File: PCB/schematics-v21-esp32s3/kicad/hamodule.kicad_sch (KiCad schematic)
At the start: 84 parts, among them J1 GND|5V, J10 Conn_01x02_Male, J11 2604-1104, J12 2604-1104, J13 EspSense, J2 Conn_01x02_Male, J3 2604-1102, J4 USB | PS, J5 GND|3.3V, J6 Conn_01x02_Male, J7 Current Jumper, J8 USB_C_Receptacle_USB2.0, J9 EspRelays, K1 AQG12205, K2 AQG12205, K3 AQG12205, K4 AQG12205, SW1 Switch, SW2 Switch, U1 LD1117AV33, U2 ESP32-S3-WROOM-2, U3 USBLC6-2SC6, U4 ULN2003A, U5 LDA210-PDIP, U6 LDA210-PDIP, U7 SHT4x

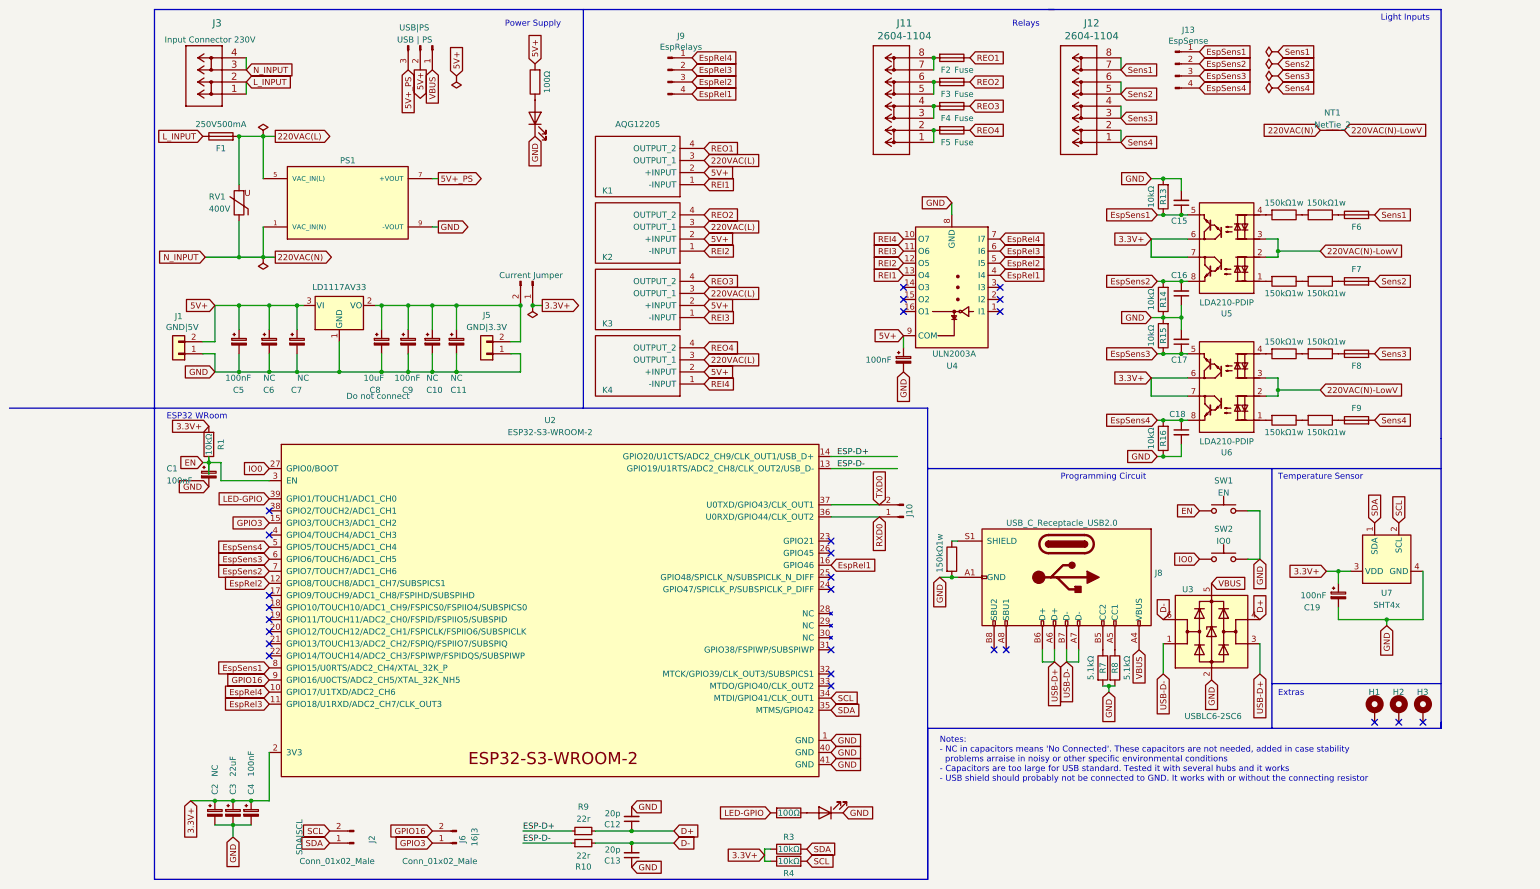
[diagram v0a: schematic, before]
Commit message: [V21] Bring DEPSI back!; expose 3rd GPIO; remove ESP unused libraries;
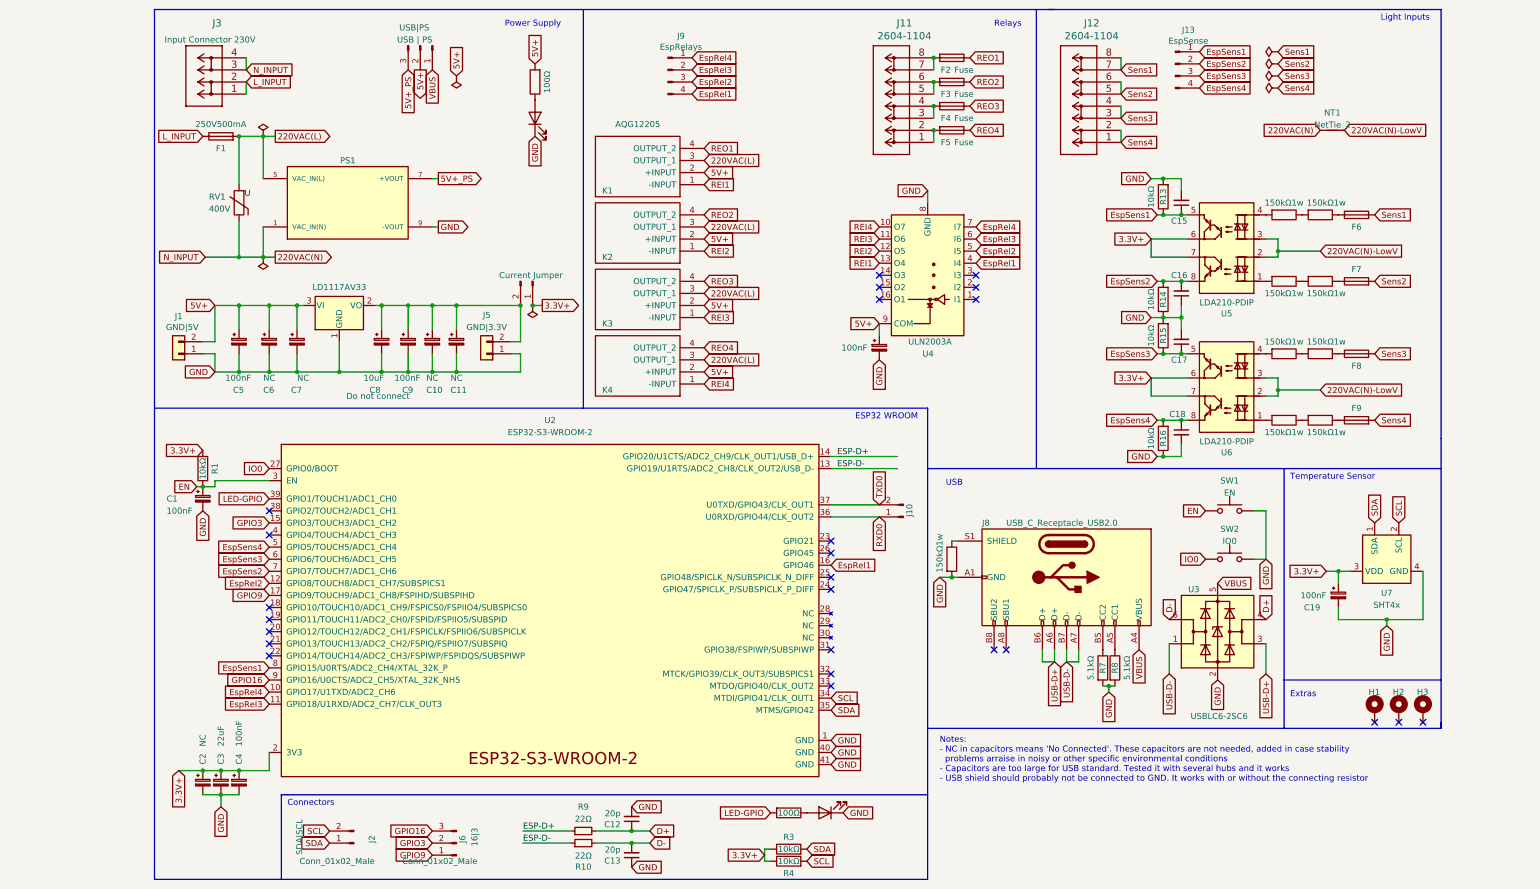
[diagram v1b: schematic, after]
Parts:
- J6: footprint Connector_PinHeader_2.54mm:PinHeader_1x02_P2.54mm_Vertical -> Connector_PinHeader_2.54mm:PinHeader_1x03_P2.54mm_Vertical; symbol Connector:Conn_01x02_Male -> Connector:Conn_01x03_Male
- R10, R9: value 22r -> 22Ω
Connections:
- net GPIO16: now also J6.3 (Pin_3); no longer J6.2 (Pin_2)
- net GPIO3: now also J6.2 (Pin_2); no longer J6.1 (Pin_1)
- net GPIO9: now reaches U2.17 (GPIO9/TOUCH9/ADC1_CH8/FSPIHD/SUBSPIHD)
- net GPIO9: now also J6.1 (Pin_1)
- no-connect marks 26 -> 25
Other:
- note added: "Connectors"
- note added: "ESP32 WROOM"
- note added: "USB"
- note removed: "ESP32 WRoom"
- note removed: "Programming Circuit"
- moved on the sheet: C1, C2, C3, C4, R1, SW1, SW2, U3, U4

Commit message: Images + Gerbers
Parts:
- added D3: BAT60A, Diode_SMD:D_SOD-323, symbol Diode:BAT60A
- renumbered C5 to C4, C4 to C5, D2 to D1, D1 to D2, J8 to J11, J3 to J2, J2 to J3, J6 to J5, J5 to J6, J9 to J8, J11 to J9, R8 to R10, R13 to R11, R14 to R12, R15 to R13, R16 to R14, R17 to R15, R18 to R16, R19 to R17, R20 to R18, R21 to R19, R5 to R2, R22 to R20, R23 to R21, R24 to R22, R9 to R3, R10 to R4, R2 to R5, R3 to R6, R4 to R7, R6 to R8, R7 to R9, U4 to U3, U3 to U4
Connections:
- net VBUS: now also D3.1 (K); no longer J11.A4 (VBUS), J11.A9 (VBUS), J11.B4 (VBUS), J11.B9 (VBUS)
- new net: D3.2 (A), J11.A4 (VBUS), J11.A9 (VBUS), J11.B4 (VBUS), J11.B9 (VBUS)
